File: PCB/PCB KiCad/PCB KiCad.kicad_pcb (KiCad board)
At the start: 2 copper layers, 80 x 120 mm, 73 parts, among them J1 ADC Debug, J2 LED Debug, J3 Qwiic, SW1 TRIGGER, SW2 MCU_RESET, U1 OPA2376xxD, U2 ADS1256IDBT, U3 LM285D-2.5, U4 AMS1117-3.3, U5 TLC59208FIPWR, Y1 7.68MHz

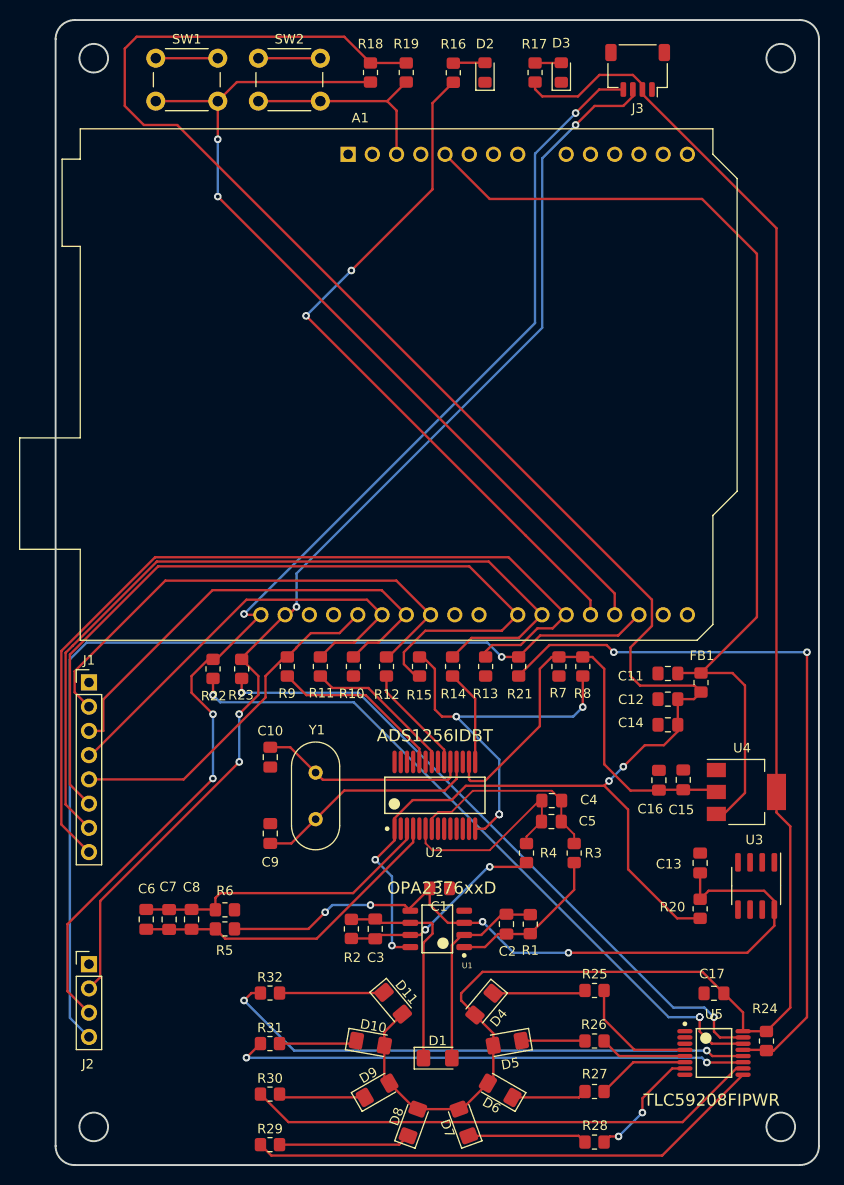
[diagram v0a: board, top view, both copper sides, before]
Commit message: routing: add ground plane, finish all tracks
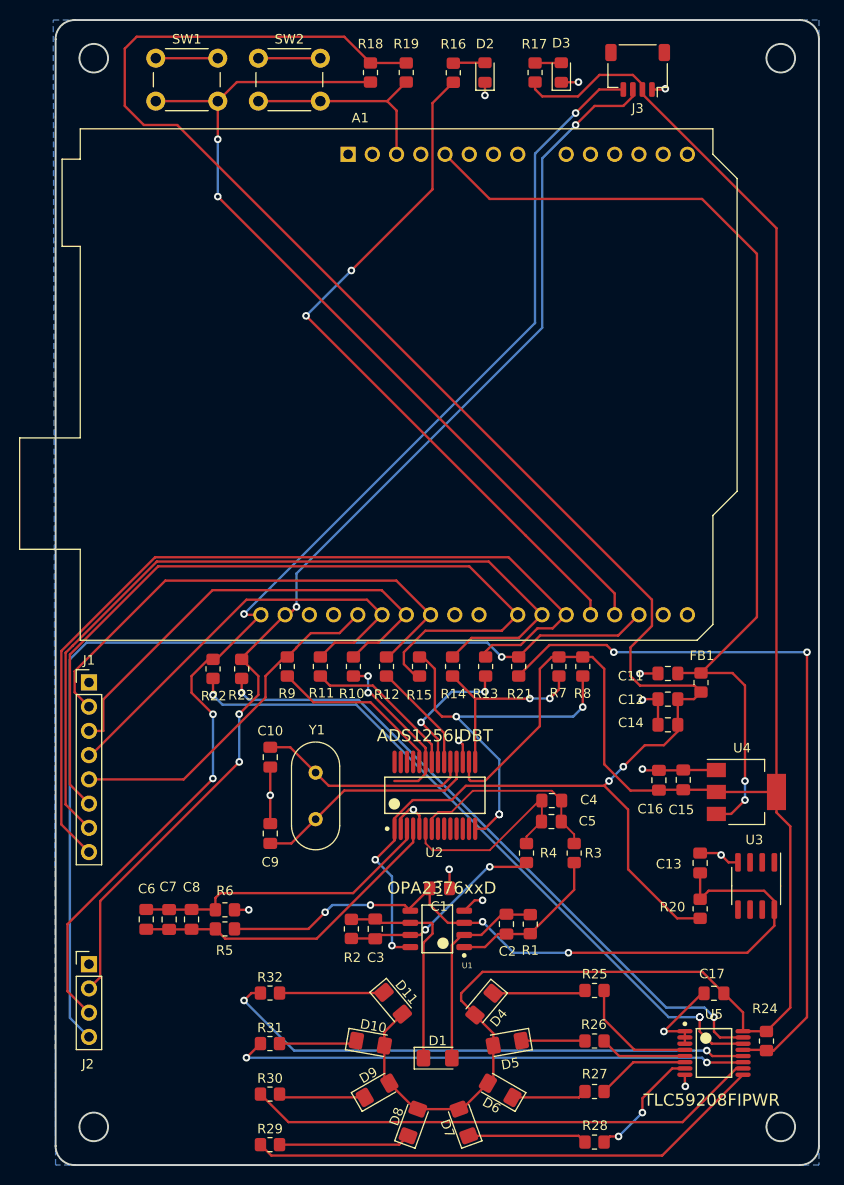
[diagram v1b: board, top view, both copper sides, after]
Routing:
- net GND: track 13.0 -> 66.0 mm, vias 0 -> 15
- net Net-(R10-Pad2): track 0.00 -> 18.0 mm, vias 0 -> 2
- net Net-(R13-Pad2): track 0.00 -> 14.6 mm, vias 0 -> 2
- net Net-(R14-Pad2): track 9.98 -> 20.6 mm, vias 0 -> 2
- net +3V3: track 237.6 -> 243.9 mm
- net Net-(C10-Pad1): track 22.0 -> 22.5 mm
- net /MCU + IO/+5V RAW: track 106.1 -> 106.6 mm, vias 0 -> 2
- added copper zone on B.Cu, net GND

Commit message: silkscreen and thicker traces
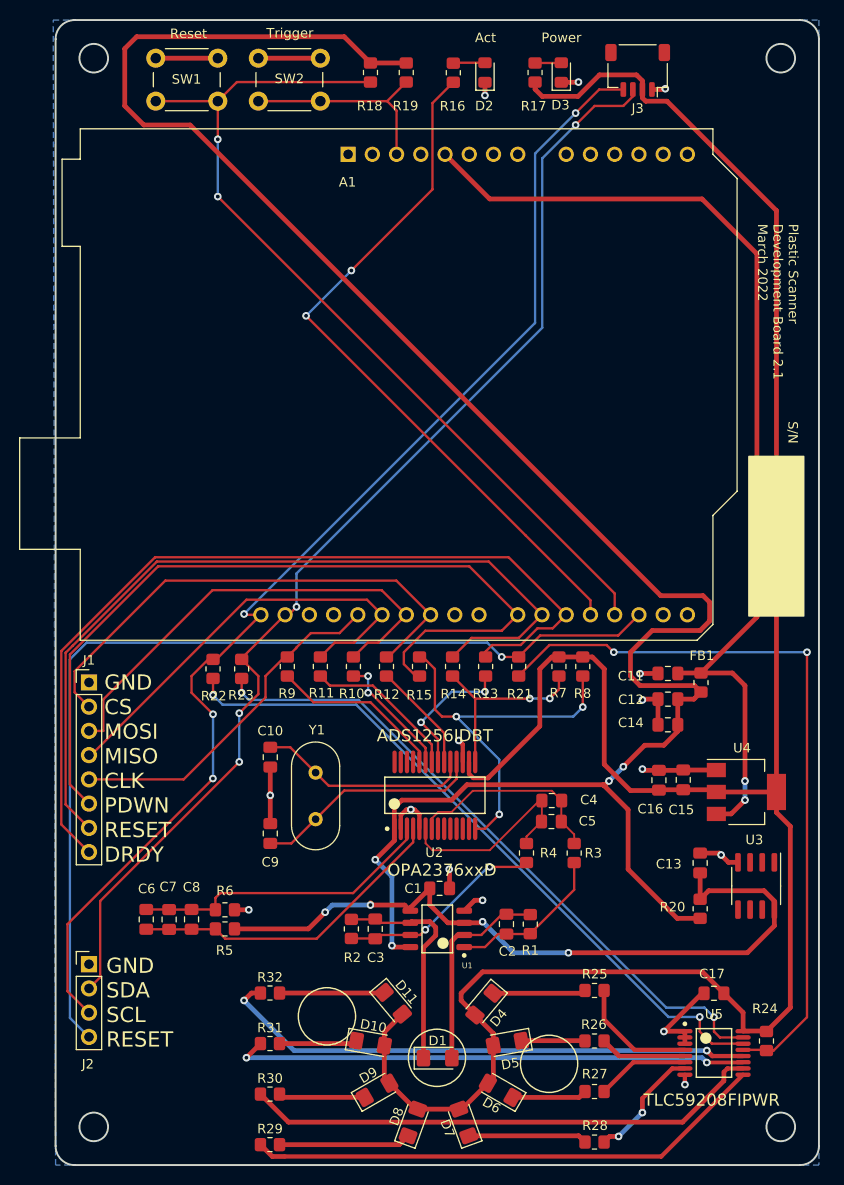
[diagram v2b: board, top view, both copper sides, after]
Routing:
- net +5V: track 206.8 -> 218.9 mm
- net Net-(R10-Pad2): track 18.0 -> 13.2 mm
- net /ADC/AIN+: track 22.4 -> 21.3 mm
- net Net-(C3-Pad2): track 22.1 -> 21.0 mm
- net +3V3: track 243.9 -> 244.8 mm
- net /MCU + IO/LED BLUE: track 75.2 -> 74.5 mm
- net Net-(R30-Pad1): track 54.1 -> 54.7 mm
- net Net-(R22-Pad2): vias 3 -> 2
- net Net-(R15-Pad2): vias 4 -> 3
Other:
- board text added: "Act"
- board text added: "GND CS MOSI MISO CLK PDWN RESET DRDY"
- board text added: "GND SDA SCL RESET"
- board text added: "Plastic Scanner Development Board 2.1 March 2022"
- board text added: "Power"
- board text added: "Reset"
- board text added: "S/N"
- board text added: "Trigger"

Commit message: Fixed mounting holes, added logo
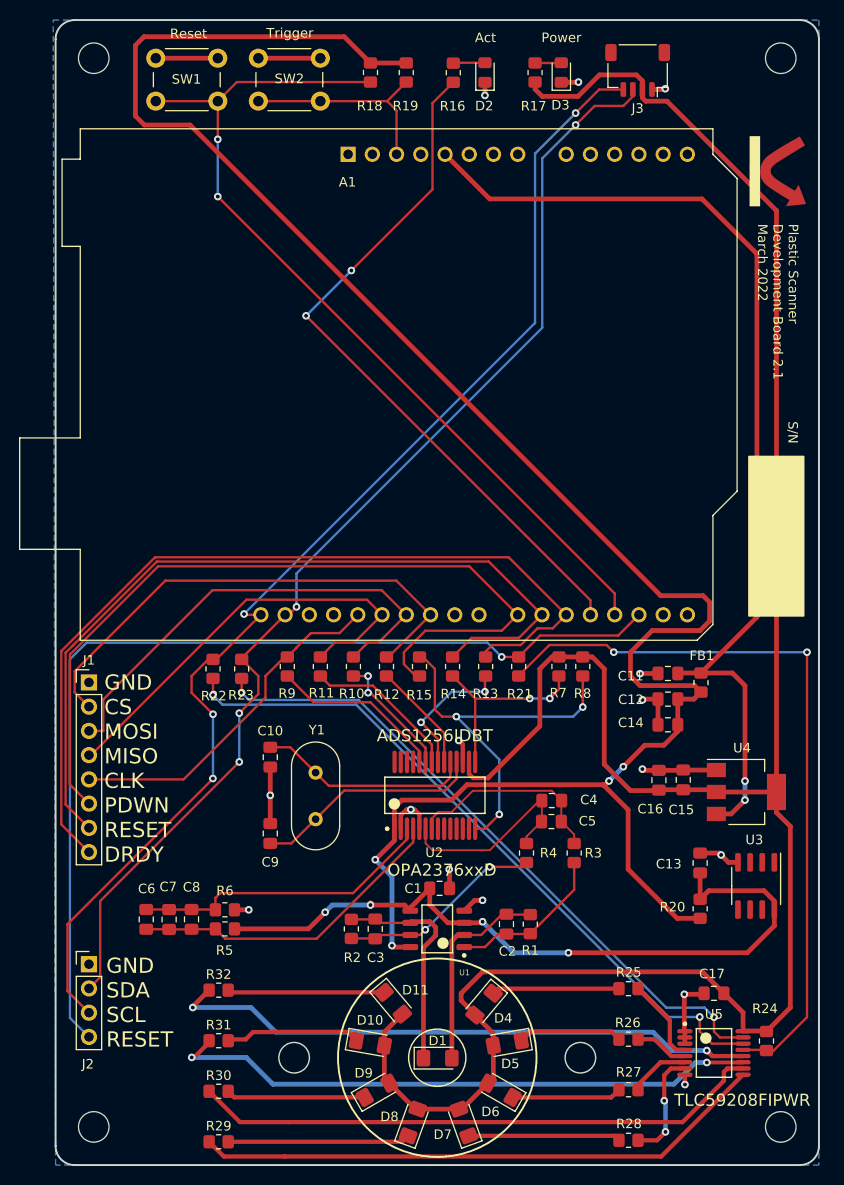
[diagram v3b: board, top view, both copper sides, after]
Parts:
- added REF**: MountingHole_3.2mm_M3, MountingHole:MountingHole_3.2mm_M3, F.Cu at (119.0, 144.0)
- added REF**: MountingHole_3.2mm_M3, MountingHole:MountingHole_3.2mm_M3, F.Cu at (119.0, 32.0)
- added REF**: MountingHole_3.2mm_M3, MountingHole:MountingHole_3.2mm_M3, F.Cu at (47.0, 144.0)
- added REF**: front_silk, plastic_scanner_logo:front_silk, F.Cu at (119.0, 43.8)
- added REF**: MountingHole_3.2mm_M3, MountingHole:MountingHole_3.2mm_M3, F.Cu at (47.0, 32.0)
- moved R29 5.39 mm to (60.1, 145.6)
- moved R30 5.39 mm to (60.1, 140.3)
- moved R32 5.39 mm to (60.1, 129.7)
- moved R31 5.39 mm to (60.1, 135.0)
- moved R25 3.56 mm to (103.0, 129.5)
- moved R26 3.56 mm to (103.0, 134.8)
- moved R27 3.56 mm to (103.0, 140.1)
- moved R28 3.56 mm to (103.0, 145.4)
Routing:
- net Net-(R31-Pad1): track 54.4 -> 62.5 mm
- net Net-(D10-Pad1): track 8.18 -> 14.2 mm
- net Net-(R32-Pad1): track 56.8 -> 62.3 mm
- net Net-(R30-Pad1): track 54.7 -> 60.2 mm
- net Net-(R29-Pad1): track 54.6 -> 60.1 mm
- net Net-(D9-Pad1): track 9.07 -> 14.6 mm
- net Net-(D11-Pad1): track 11.0 -> 16.4 mm
- net Net-(D8-Pad1): track 13.9 -> 19.1 mm
- net Net-(D5-Pad1): track 6.69 -> 11.0 mm
- net Net-(R25-Pad1): track 12.8 -> 8.98 mm
- net Net-(D4-Pad1): track 9.74 -> 13.4 mm
- net Net-(D6-Pad1): track 7.85 -> 11.5 mm
- net Net-(R26-Pad1): track 9.12 -> 5.64 mm
- net Net-(D7-Pad1): track 12.5 -> 15.9 mm
- net Net-(R27-Pad1): track 9.74 -> 6.41 mm
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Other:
- outline, holes or cut-outs redrawn

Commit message: PCB at time of order
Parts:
- added 2.5v: TestPoint_Pad_D2.0mm, TestPoint:TestPoint_Pad_D2.0mm, F.Cu at (102.3, 122.0)
- added 3.3v: TestPoint_Pad_D2.0mm, TestPoint:TestPoint_Pad_D2.0mm, F.Cu at (119.3, 100.3)
- added 5.0v: TestPoint_Pad_D2.0mm, TestPoint:TestPoint_Pad_D2.0mm, F.Cu at (97.8, 105.0)
- added C15: 10, Capacitor_SMD:C_0805_2012Metric_Pad1.18x1.45mm_HandSolder, F.Cu at (106.2, 112.0)
- R17: value 82 -> 150
- renumbered REF** to ?, C15 to C16, C16 to C17, C17 to C18, R19 to R18, R18 to R19, SW2 to SW1, SW1 to SW2
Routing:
- net GND: track 63.9 -> 47.5 mm, vias 15 -> 43
- net /MCU + IO/+5V RAW: track 106.6 -> 112.7 mm, vias 2 -> 0
- net +3V3: track 244.8 -> 240.5 mm
- net +5V: track 217.5 -> 220.7 mm
- net +2V5: track 78.1 -> 81.3 mm
- net Net-(R31-Pad1): track 62.5 -> 64.6 mm
- added copper zone on F.Cu, net GND
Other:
- board text added: "JLCJLCJLCJLC"

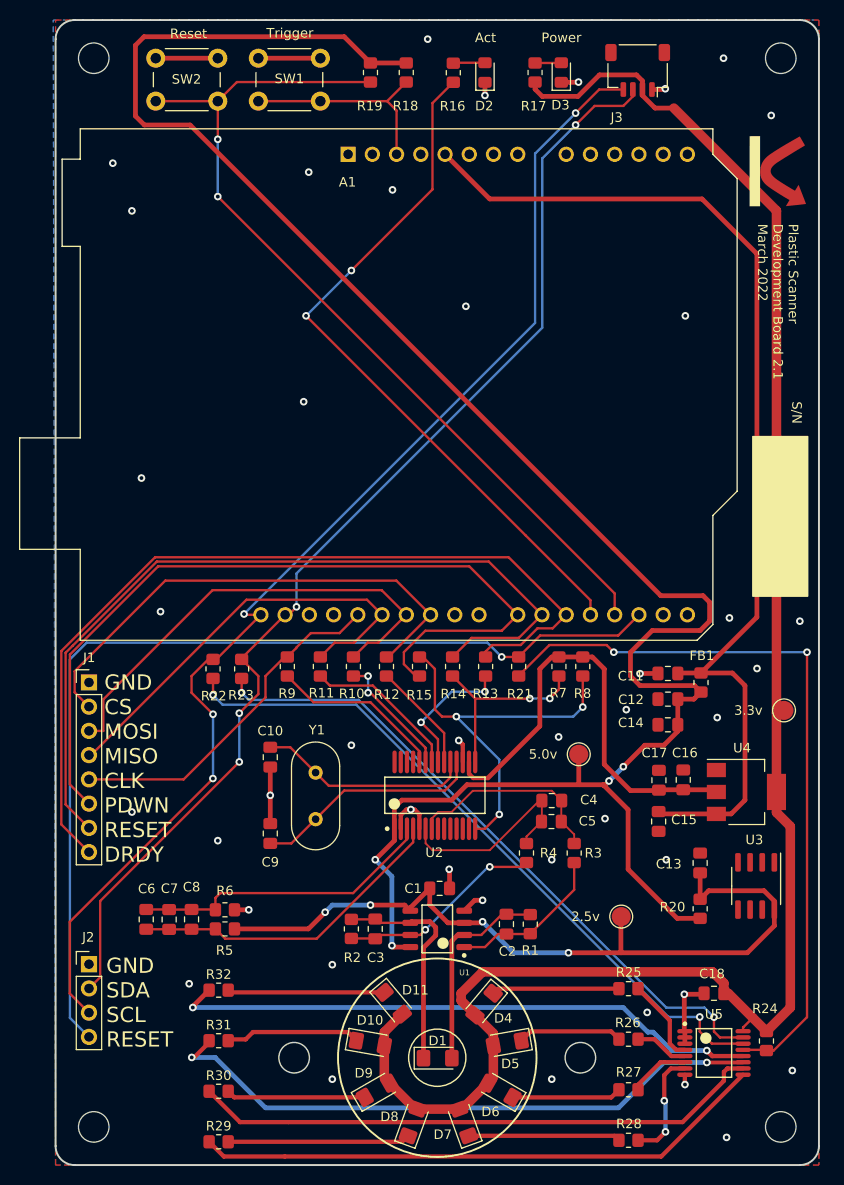
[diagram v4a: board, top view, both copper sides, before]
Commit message: fixes issue #09 and adds gnd testpad to make testing easier
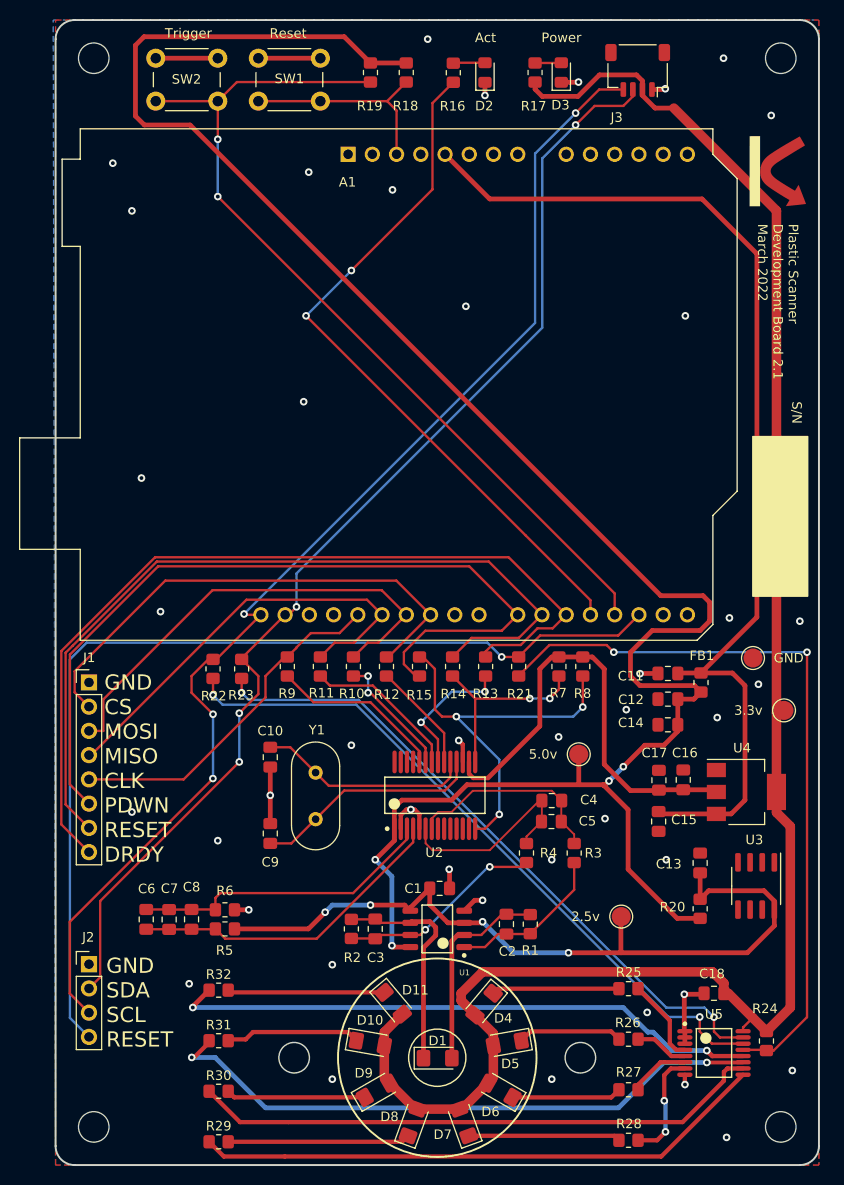
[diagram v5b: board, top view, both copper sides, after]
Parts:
- added GND: TestPoint_Pad_D2.0mm, TestPoint:TestPoint_Pad_D2.0mm, F.Cu at (116.1, 94.9)
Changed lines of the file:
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@@
     )
+  )
+  (footprint "TestPoint:TestPoint_Pad_D2.0mm" (layer "F.Cu")
+    (at 116.09 94.86)
+    (descr "SMD pad as test Point, diameter 2.0mm")
+    (tags "test point SMD pad")
+    (attr exclude_from_pos_files exclude_from_bom)
+    (fp_text reference "GND" (at 3.74 0) (layer "F.SilkS")
+      (effects (font (size 1 1) (thickness 0.15)))
+    )
+    (fp_text value "TestPoint_Pad_D2.0mm" (at 0 2.05) (layer "F.Fab")
+      (effects (font (size 1 1) (thickness 0.15)))
+    )
+    (fp_text user "${REFERENCE}" (at 0 -2) (layer "F.Fab")
+      (effects (font (size 1 1) (thickness 0.15)))
+    )
+    (fp_circle (center 0 0) (end 0 1.2) (layer "F.SilkS") (width 0.12) (fill none))
+    (fp_circle (center 0 0) (end 1.5 0) (layer "F.CrtYd") (width 0.05) (fill none))
+    (pad "4" smd circle (at 0 0) (size 2 2) (layers "F.Cu" "F.Mask")
+      (net 6 "GND"))
   )
   (footprint "LED_SMD:LED_1206_3216Metric_Pad1.42x1.75mm_HandSolder" (layer "F.Cu")
@@
     (effects (font (size 1 1) (thickness 0.15)))
   )
-  (gr_text "Reset" (at 56.93 29.43) (layer "F.SilkS")
+  (gr_text "Reset" (at 67.37 29.39) (layer "F.SilkS")
     (effects (font (size 1 1) (thickness 0.15)))
   )
@@
     (effects (font (size 1 1) (thickness 0.15)))
   )
-  (gr_text "Trigger" (at 67.56 29.37) (layer "F.SilkS")
+  (gr_text "Trigger" (at 56.92 29.39) (layer "F.SilkS")
     (effects (font (size 1 1) (thickness 0.15)))
   )
@@
   (via (at 78.31 45.8) (size 0.8) (drill 0.4) (layers "F.Cu" "B.Cu") (free) (net 6))
   (via (at 80.23 110.74) (size 0.8) (drill 0.4) (layers "F.Cu" "B.Cu") (net 6))
+  (via (at 116.66 97.61) (size 0.8) (drill 0.4) (layers "F.Cu" "B.Cu") (free) (net 6))
   (via (at 113.32 145.1) (size 0.8) (drill 0.4) (layers "F.Cu" "B.Cu") (free) (net 6))
   (via (at 109 59) (size 0.8) (drill 0.4) (layers "F.Cu" "B.Cu") (free) (net 6))
@@
   (via (at 51 111) (size 0.8) (drill 0.4) (layers "F.Cu" "B.Cu") (free) (net 6))
   (via (at 113.62 90.66) (size 0.8) (drill 0.4) (layers "F.Cu" "B.Cu") (free) (net 6))
-  (via (at 116.51 95.96) (size 0.8) (drill 0.4) (layers "F.Cu" "B.Cu") (free) (net 6))
   (via (at 97.8 34.5) (size 0.8) (drill 0.4) (layers "F.Cu" "B.Cu") (net 6))
   (via (at 63.25 121.25) (size 0.8) (drill 0.4) (layers "F.Cu" "B.Cu") (net 6))
